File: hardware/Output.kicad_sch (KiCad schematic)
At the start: 9 parts, among them Q801 2N7002, Q802 AO4407A

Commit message: Tracing 2
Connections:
- net VIN: now also Q802.2 (S), Q802.3 (S)
- net INA226_OUT/VIN+ renamed INA226_OUT/VIN
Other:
- sheet INA226_OUT ports: added VIN, VOUT; removed VIN+, VIN-
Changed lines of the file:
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@@
-			)
-		)
-		(pin "VIN+" input
-			(at 146.05 100.33 180)
-			(effects
-				(font
-					(size 1.27 1.27)
-				)
-				(justify left)
 			)
 		)
@@
 			)
 		)
-		(pin "VIN-" input
-			(at 166.37 102.87 0)
-			(effects
-				(font
-					(size 1.27 1.27)
-				)
-				(justify right)
-			)
-		)
 		(pin "A0" input
 			(at 146.05 105.41 180)
@@
 			)
 		)
+		(pin "VIN" input
+			(at 146.05 100.33 180)
+			(effects
+				(font
+					(size 1.27 1.27)
+				)
+				(justify left)
+			)
+		)
+		(pin "VOUT" input
+			(at 166.37 102.87 0)
+			(effects
+				(font
+					(size 1.27 1.27)
+				)
+				(justify right)
+			)
+		)

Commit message: Tracing 3
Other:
- sheet INA226_OUT ports: added ALERT; removed none
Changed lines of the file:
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@@
+	(wire
+		(pts
+			(xy 166.37 106.68) (xy 177.8 106.68)
+		)
+		(stroke
+			(width 0)
+			(type default)
+		)
+	)
 	(wire
 		(pts
@@
 		)
 	)
+	(hierarchical_label "ALERT"
+		(shape output)
+		(at 177.8 106.68 0)
+		(effects
+			(font
+				(size 1.27 1.27)
+			)
+			(justify left)
+		)
+	)
 	(hierarchical_label "INA226_A0"
 		(shape input)
@@
 			(effects
 				(font
+					(size 1.27 1.27)
+				)
+				(justify right)
+			)
+		)
+		(pin "ALERT" input
+			(at 166.37 106.68 0)
+			(effects
+				(font

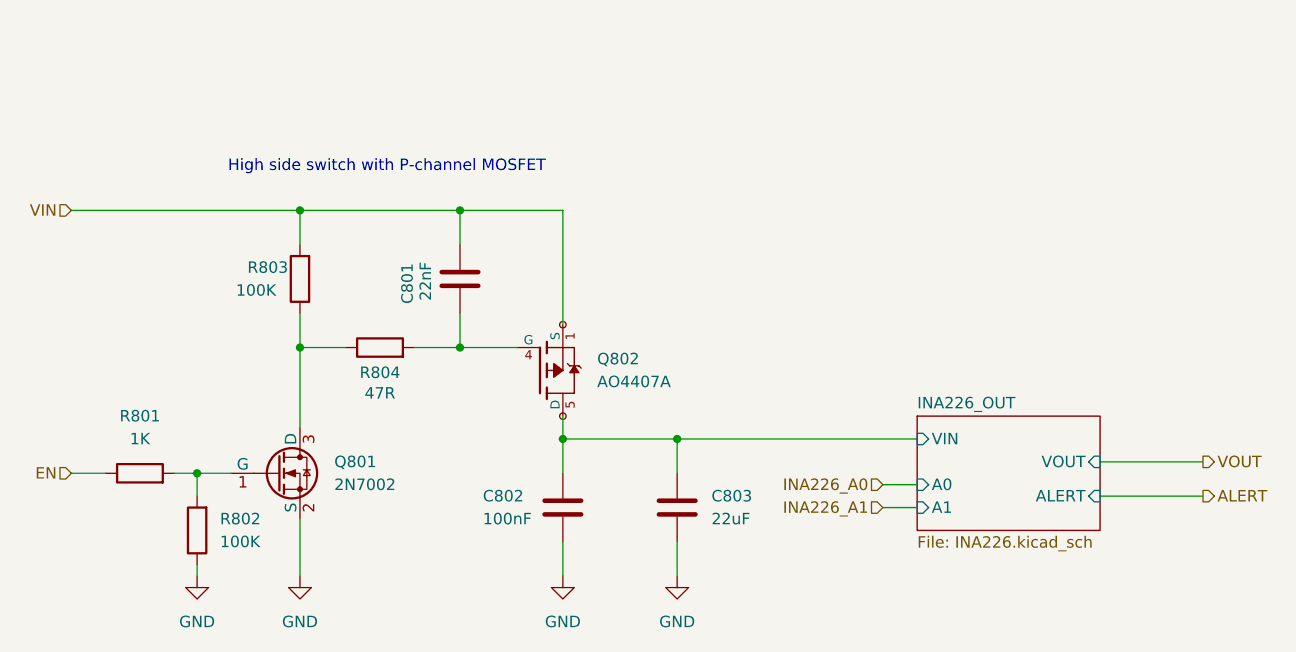
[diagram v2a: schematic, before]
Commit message: thermal relief
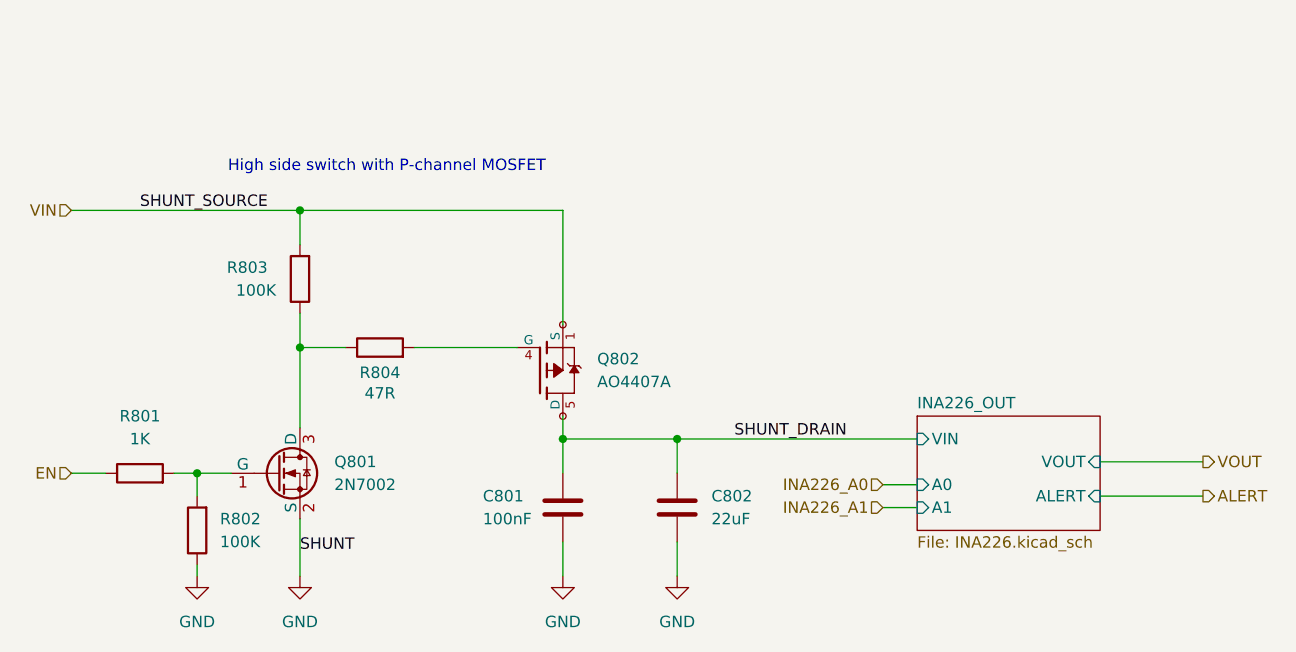
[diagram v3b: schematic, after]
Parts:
- removed C801: 22nF, Capacitor_SMD:C_0805_2012Metric, symbol Device:C
- renumbered C802 to C801, C803 to C802
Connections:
- net INA226_OUT/VIN renamed SHUNT_DRAIN
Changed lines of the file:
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@@
-	)
-	(junction
-		(at 95.25 74.93)
-		(diameter 0)
-		(color 0 0 0 0)
 	)
 	(junction
@@
 	)
 	(junction
-		(at 95.25 90.17)
-		(diameter 0)
-		(color 0 0 0 0)
-	)
-	(junction
 		(at 66.04 104.14)
 		(diameter 0)
@@
 	(wire
 		(pts
-			(xy 95.25 90.17) (xy 101.6 90.17)
+			(xy 90.17 90.17) (xy 101.6 90.17)
 		)
 		(stroke
@@
 	(wire
 		(pts
-			(xy 95.25 74.93) (xy 106.68 74.93)
-		)
-		(stroke
-			(width 0)
-			(type default)
-		)
-	)
-	(wire
-		(pts
-			(xy 95.25 78.74) (xy 95.25 74.93)
-		)
-		(stroke
-			(width 0)
-			(type default)
-		)
-	)
-	(wire
-		(pts
-			(xy 90.17 90.17) (xy 95.25 90.17)
-		)
-		(stroke
-			(width 0)
-			(type default)
-		)
-	)
-	(wire
-		(pts
-			(xy 95.25 86.36) (xy 95.25 90.17)
+			(xy 77.47 74.93) (xy 106.68 74.93)
 		)
 		(stroke
@@
 		)
 	)
-	(wire
-		(pts
-			(xy 77.47 74.93) (xy 95.25 74.93)
-		)
-		(stroke
-			(width 0)
-			(type default)
+	(label "SHUNT_DRAIN"
+		(at 125.73 100.33 0)
+		(effects
+			(font
+				(size 1.27 1.27)
+			)
+			(justify left bottom)
+		)
+	)
+	(label "SHUNT"
+		(at 77.47 113.03 0)
+		(effects
+			(font
+				(size 1.27 1.27)
+			)
+			(justify left bottom)
+		)
+	)
+	(label "SHUNT_SOURCE"
+		(at 59.69 74.93 0)
+		(effects
+			(font
+				(size 1.27 1.27)
+			)
+			(justify left bottom)
 		)
 	)
@@
 		(dnp no)
 		(property "Reference" "R803"
-			(at 71.628 81.28 0)
+			(at 69.342 81.28 0)
 			(effects
 				(font
@@
 		(dnp no)
 		(fields_autoplaced yes)
-		(property "Reference" "C803"
+		(property "Reference" "C802"
 			(at 123.19 106.6799 0)
 			(effects
@@
 			(project "NosVolt"
 				(path "/2a3ef4c2-927a-45cd-a4f2-5ee83a7e9444/56c5dda2-1e55-4d6c-a70d-c1acd647cefd"
-					(reference "C1103")
+					(reference "C1102")
 					(unit 1)
 				)
 				(path "/2a3ef4c2-927a-45cd-a4f2-5ee83a7e9444/865d6fe0-7870-4134-be7f-c35221518457"
-					(reference "C803")
+					(reference "C802")
 					(unit 1)
 				)
 				(path "/2a3ef4c2-927a-45cd-a4f2-5ee83a7e9444/b3941ffe-e8e1-48f3-a016-360d76a87258"
-					(reference "C903")
+					(reference "C902")
 					(unit 1)
 				)
@@
 		(on_board yes)
 		(dnp no)
-		(property "Reference" "C802"
+		(property "Reference" "C801"
 			(at 97.79 106.68 0)
 			(effects
@@
 			(effects
 				(font
-					(size 1.27 1.27)
-				)
-				(hide yes)
-			)
-		)
-		(pin "1"
-		)
-		(pin "2"
-		)
-		(instances
-			(project "NosVolt"
-				(path "/2a3ef4c2-927a-45cd-a4f2-5ee83a7e9444/56c5dda2-1e55-4d6c-a70d-c1acd647cefd"
-					(reference "C1102")
-					(unit 1)
-				)
-				(path "/2a3ef4c2-927a-45cd-a4f2-5ee83a7e9444/865d6fe0-7870-4134-be7f-c35221518457"
-					(reference "C802")
-					(unit 1)
-				)
-				(path "/2a3ef4c2-927a-45cd-a4f2-5ee83a7e9444/b3941ffe-e8e1-48f3-a016-360d76a87258"
-					(reference "C902")
-					(unit 1)
-				)
-			)
-		)
-	)
-	(symbol
-		(lib_id "Device:C")
-		(at 95.25 82.55 180)
-		(unit 1)
-		(exclude_from_sim no)
-		(in_bom yes)
-		(on_board yes)
-		(dnp no)
-		(property "Reference" "C801"
-			(at 89.408 83.058 90)
-			(effects
-				(font
-					(size 1.27 1.27)
-				)
-			)
-		)
-		(property "Value" "22nF"
-			(at 91.44 82.804 90)
-			(effects
-				(font
-					(size 1.27 1.27)
-				)
-			)
-		)
-		(property "Footprint" "Capacitor_SMD:C_0805_2012Metric"
-			(at 94.2848 78.74 0)
-			(effects
-				(font
-					(size 1.27 1.27)
-				)
-				(hide yes)
-			)
-		)
-		(property "Datasheet" "~"
-			(at 95.25 82.55 0)
-			(effects
-				(font
-					(size 1.27 1.27)
-				)
-				(hide yes)
-			)
-		)
-		(property "Description" "Unpolarized capacitor"
-			(at 95.25 82.55 0)
-			(effects
-				(font

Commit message: tracing
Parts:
- added NT801: NetTie_2, symbol Device:NetTie_2
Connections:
- net VIN: now also NT801.2; no longer R803.2
- new net: NT801.1, R803.2

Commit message: fix errors 2
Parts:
- NT801: footprint (none) -> NetTie:NetTie-2_SMD_Pad0.5mm
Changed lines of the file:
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@@
 			)
 		)
-		(property "Footprint" ""
+		(property "Footprint" "NetTie:NetTie-2_SMD_Pad0.5mm"
 			(at 77.47 72.39 0)
 			(effects

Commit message: reanotate
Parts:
- renumbered C801 to C501, C802 to C503, NT801 to NT501, Q801 to Q501, Q802 to Q502, R801 to R501, R802 to R502, R803 to R503, R804 to R505

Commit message: hand soldering footprints and led
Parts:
- C501: footprint Capacitor_SMD:C_0603_1608Metric -> Capacitor_SMD:C_0603_1608Metric_Pad1.08x0.95mm_HandSolder
- C503: footprint Capacitor_SMD:C_0805_2012Metric -> Capacitor_SMD:C_0805_2012Metric_Pad1.18x1.45mm_HandSolder
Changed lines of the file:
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@@
 			)
 		)
-		(property "Footprint" "Capacitor_SMD:C_0805_2012Metric"
+		(property "Footprint" "Capacitor_SMD:C_0805_2012Metric_Pad1.18x1.45mm_HandSolder"
 			(at 120.3452 111.76 0)
 			(effects
@@
 			)
 		)
-		(property "Footprint" "Capacitor_SMD:C_0603_1608Metric"
+		(property "Footprint" "Capacitor_SMD:C_0603_1608Metric_Pad1.08x0.95mm_HandSolder"
 			(at 107.6452 111.76 0)
 			(effects

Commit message: PWR_FLG
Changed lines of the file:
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@@
-		)
-	)
-	(label "SHUNT"
-		(at 77.47 113.03 0)
-		(effects
-			(font
-				(size 1.27 1.27)
-			)
-			(justify left bottom)
-		)
-	)
-	(label "SHUNT_SOURCE"
-		(at 59.69 64.77 0)
-		(effects
-			(font
-				(size 1.27 1.27)
-			)
-			(justify left bottom)
 		)
 	)
